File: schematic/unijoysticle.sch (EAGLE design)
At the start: 8 parts, among them IC1 4066N, IC2 4066N, IC3 4066N, J1 DB9, J2 DB9, J3 POWER_JACKSLT

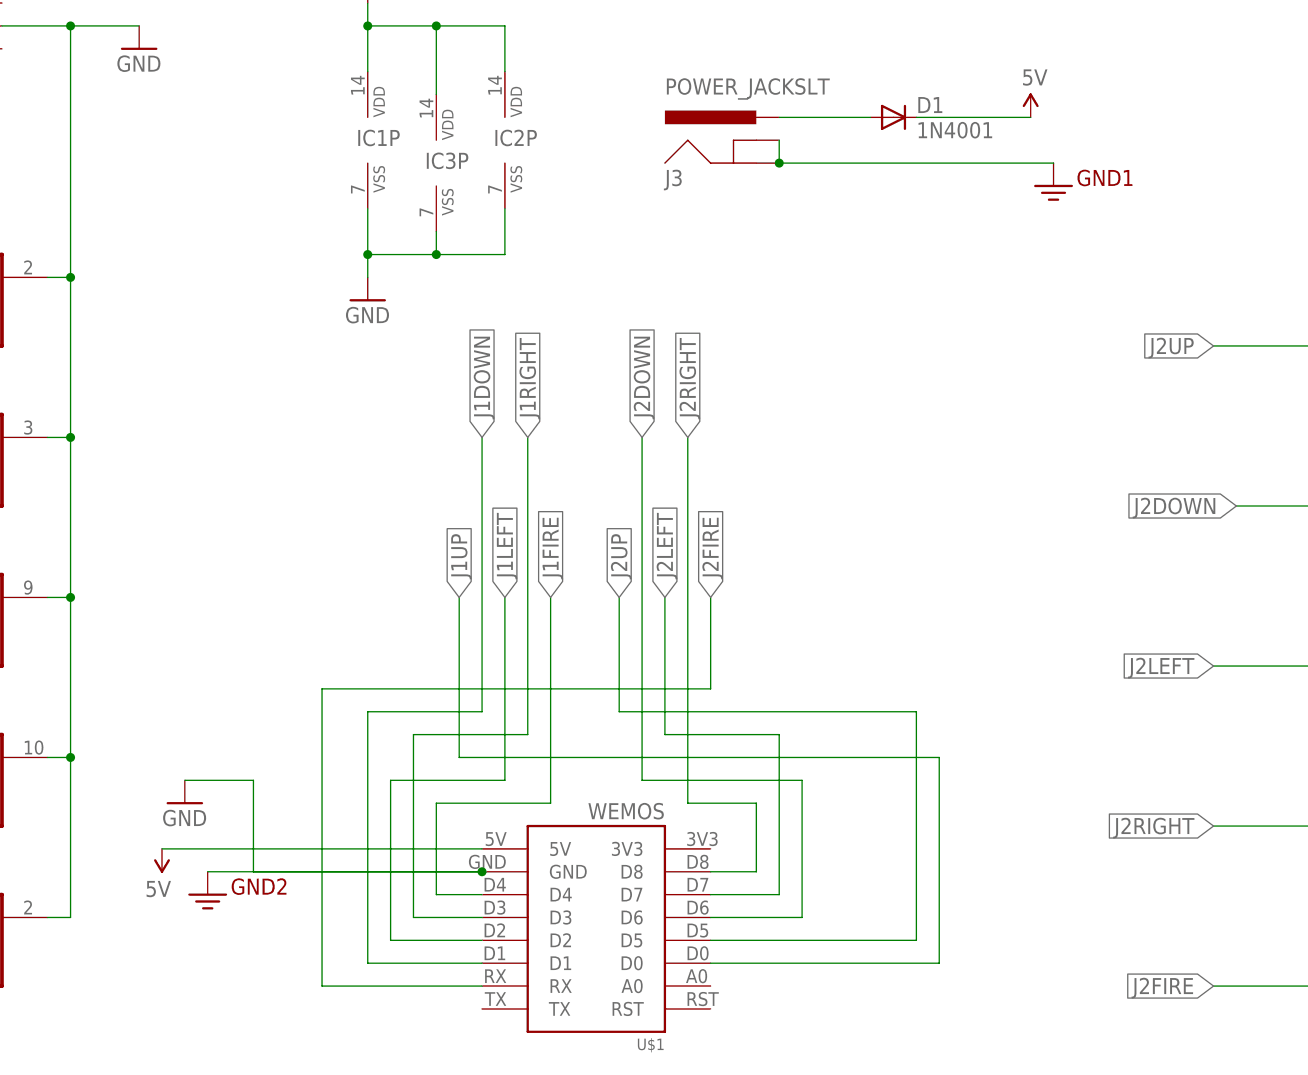
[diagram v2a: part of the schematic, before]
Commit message: sharing the same ground for all components
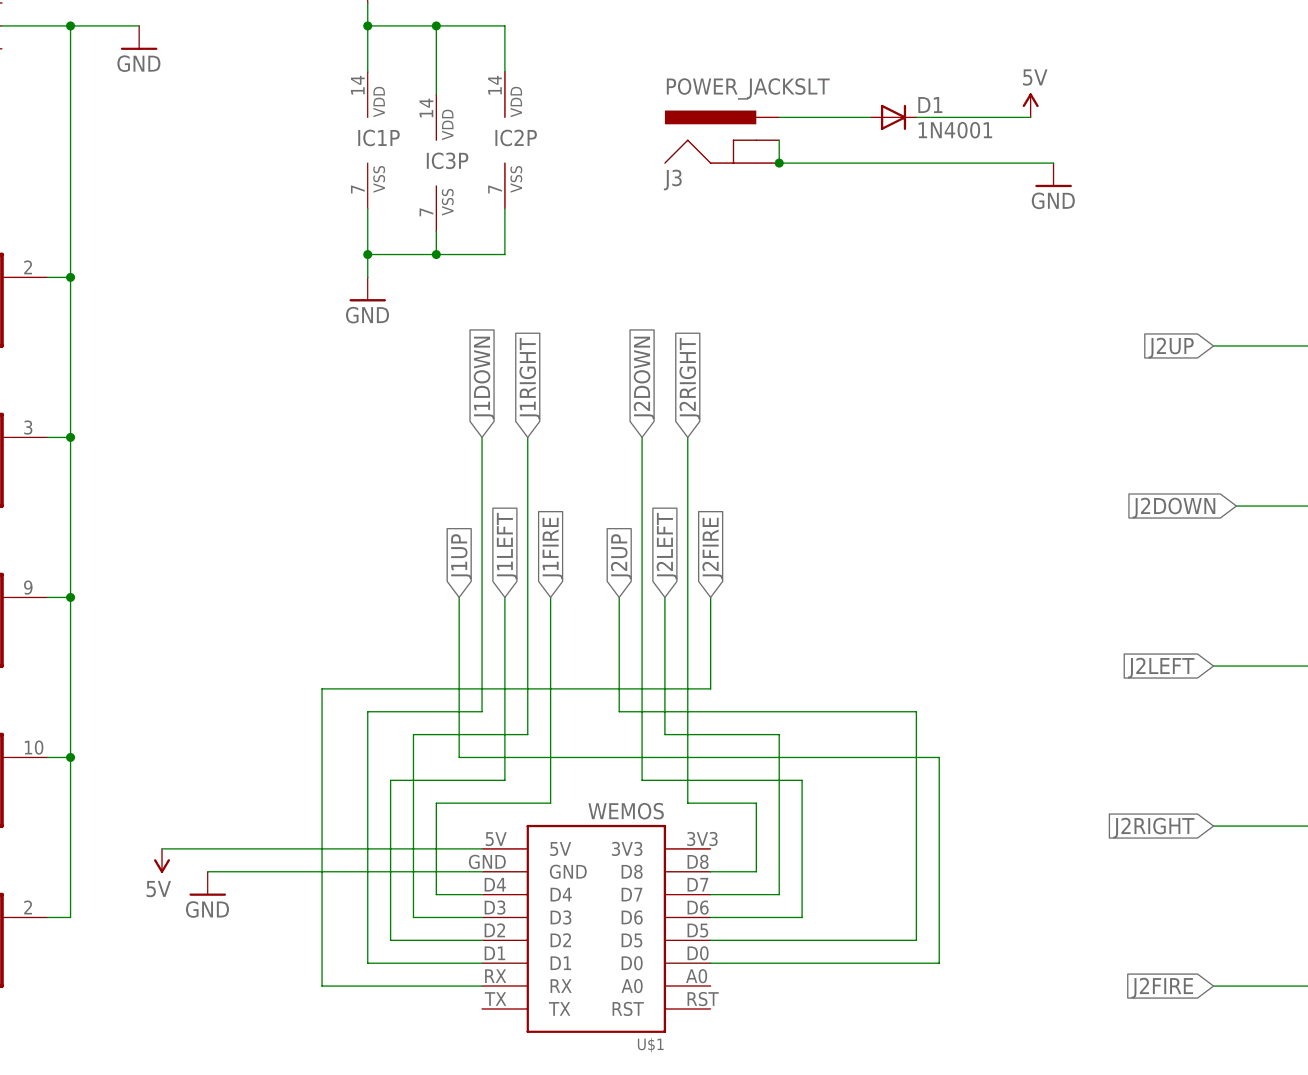
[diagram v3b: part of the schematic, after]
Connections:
- removed net 3.3V: J3.GND, J3.GNDBREAK
- net GND: now also J3.GND, J3.GNDBREAK
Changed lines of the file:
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@@
 <part name="SUPPLY1" library="SparkFun-Aesthetics" deviceset="5V" device=""/>
 <part name="SUPPLY2" library="SparkFun-Aesthetics" deviceset="5V" device=""/>
-<part name="GND1" library="SparkFun-Aesthetics" deviceset="GND2" device=""/>
-<part name="GND2" library="SparkFun-Aesthetics" deviceset="GND2" device=""/>
 <part name="J1" library="riq-connectors" deviceset="DB9" device="FEMALE" value="DB9">
 <attribute name="MF" value=""/>
@@
 <part name="GND6" library="SparkFun-Aesthetics" deviceset="GND" device=""/>
 <part name="U$1" library="1455413453956-wemos" deviceset="WEMOS" device=""/>
+<part name="GND1" library="supply1" deviceset="GND" device=""/>
 </parts>
 <sheets>
@@
 <instance part="IC1" gate="P" x="101.6" y="142.24"/>
 <instance part="IC3" gate="P" x="109.22" y="139.7"/>
-<instance part="GND3" gate="1" x="81.28" y="68.58"/>
+<instance part="GND3" gate="1" x="83.82" y="58.42"/>
 <instance part="GND4" gate="1" x="101.6" y="124.46"/>
 <instance part="IC2" gate="A" x="53.34" y="53.34">
@@
 <instance part="SUPPLY1" gate="G$1" x="175.26" y="144.78"/>
 <instance part="SUPPLY2" gate="G$1" x="78.74" y="63.5" rot="R180"/>
-<instance part="GND1" gate="G$1" x="177.8" y="137.16"/>
-<instance part="GND2" gate="G$1" x="83.82" y="58.42"/>
 <instance part="J1" gate="G$1" x="53.34" y="157.48">
 <attribute name="OC_NEWARK" x="53.34" y="157.48" size="1.778" layer="96" display="off"/>
@@
 <instance part="GND6" gate="1" x="76.2" y="152.4"/>
 <instance part="U$1" gate="G$1" x="134.62" y="66.04" rot="R180"/>
+<instance part="GND1" gate="1" x="177.8" y="137.16"/>
 </instances>
 <busses>
@@
 <segment>
 <pinref part="GND3" gate="1" pin="GND"/>
-<pinref part="GND2" gate="G$1" pin="3.3V"/>
+<pinref part="U$1" gate="G$1" pin="GND"/>
 <wire x1="83.82" y1="60.96" x2="114.3" y2="60.96" width="0.1524" layer="91"/>
-<pinref part="U$1" gate="G$1" pin="GND"/>
-<wire x1="81.28" y1="71.12" x2="88.9" y2="71.12" width="0.1524" layer="91"/>
-<wire x1="88.9" y1="71.12" x2="88.9" y2="60.96" width="0.1524" layer="91"/>
-<wire x1="88.9" y1="60.96" x2="114.3" y2="60.96" width="0.1524" layer="91"/>
-<junction x="114.3" y="60.96"/>
 </segment>
 <segment>
@@
 <pinref part="GND6" gate="1" pin="GND"/>
 </segment>
+<segment>
+<wire x1="147.32" y1="142.24" x2="147.32" y2="139.7" width="0.1524" layer="91"/>
+<wire x1="147.32" y1="139.7" x2="177.8" y2="139.7" width="0.1524" layer="91"/>
+<pinref part="J3" gate="G$1" pin="GNDBREAK"/>
+<pinref part="J3" gate="G$1" pin="GND"/>
+<junction x="147.32" y="139.7"/>
+<pinref part="GND1" gate="1" pin="GND"/>
+</segment>
 </net>
 <net name="VCC" class="0">
@@
 </segment>
 </net>
-<net name="3.3V" class="0">
-<segment>
-<wire x1="147.32" y1="142.24" x2="147.32" y2="139.7" width="0.1524" layer="91"/>
-<wire x1="147.32" y1="139.7" x2="177.8" y2="139.7" width="0.1524" layer="91"/>
-<pinref part="GND1" gate="G$1" pin="3.3V"/>
-<pinref part="J3" gate="G$1" pin="GNDBREAK"/>
-<pinref part="J3" gate="G$1" pin="GND"/>
-<junction x="147.32" y="139.7"/>
-</segment>
-</net>

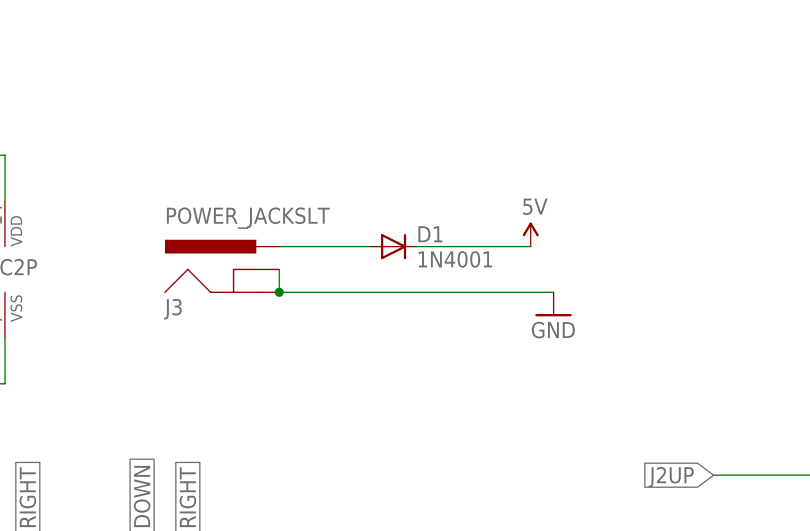
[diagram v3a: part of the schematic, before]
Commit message: removed diode
apparently not needed:
http://forum.wemos.cc/topic/343/power-the-board-with-both-usb-and-vin-pin-at-the-same-time
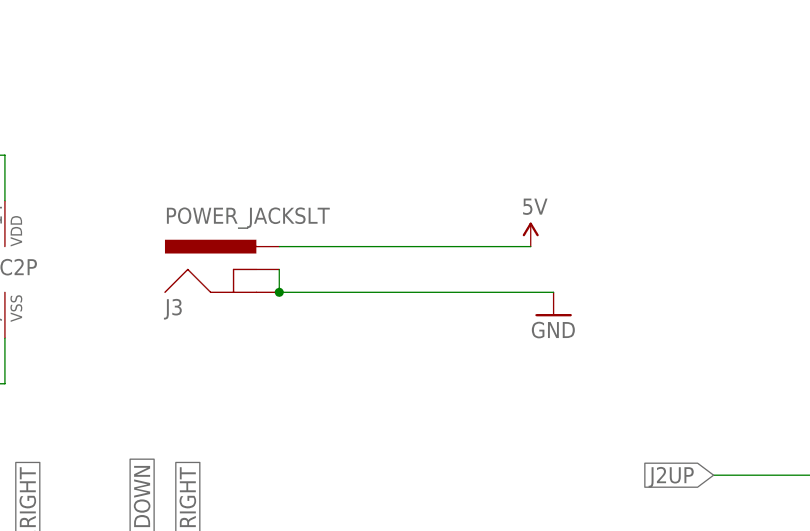
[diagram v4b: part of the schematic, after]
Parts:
- removed D1: 1N4001, diode:1N4004
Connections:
- removed net N$23: D1.A, J3.PWR
- net 5V: now also J3.PWR; no longer D1.C
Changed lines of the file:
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@@
 <attribute name="OC_NEWARK" value="76C3574"/>
-</part>
-<part name="D1" library="diode" deviceset="1N4004" device="" value="1N4001">
-<attribute name="MF" value="NTE ELECTRONICS"/>
-<attribute name="MPN" value="1N4001"/>
-<attribute name="OC_NEWARK" value="10M8464"/>
 </part>
 <part name="SUPPLY1" library="SparkFun-Aesthetics" deviceset="5V" device=""/>
@@
 <instance part="IC2" gate="B" x="233.68" y="50.8"/>
 <instance part="IC2" gate="P" x="116.84" y="142.24"/>
-<instance part="D1" gate="1" x="160.02" y="144.78">
-<attribute name="OC_NEWARK" x="160.02" y="144.78" size="1.778" layer="96" display="off"/>
-<attribute name="MF" x="160.02" y="144.78" size="1.778" layer="96" display="off"/>
-<attribute name="MPN" x="160.02" y="144.78" size="1.778" layer="96" display="off"/>
-</instance>
 <instance part="SUPPLY1" gate="G$1" x="175.26" y="144.78"/>
 <instance part="SUPPLY2" gate="G$1" x="78.74" y="63.5" rot="R180"/>
@@
 </segment>
 </net>
-<net name="N$23" class="1">
-<segment>
-<wire x1="147.32" y1="144.78" x2="157.48" y2="144.78" width="0.1524" layer="91"/>
-<pinref part="D1" gate="1" pin="A"/>
+<net name="5V" class="0">
+<segment>
+<pinref part="SUPPLY1" gate="G$1" pin="5V"/>
+<wire x1="147.32" y1="144.78" x2="175.26" y2="144.78" width="0.1524" layer="91"/>
 <pinref part="J3" gate="G$1" pin="PWR"/>
 </segment>
-</net>
-<net name="5V" class="0">
-<segment>
-<wire x1="162.56" y1="144.78" x2="175.26" y2="144.78" width="0.1524" layer="91"/>
-<pinref part="D1" gate="1" pin="C"/>
-<pinref part="SUPPLY1" gate="G$1" pin="5V"/>
-</segment>
-<segment>
+<segment>

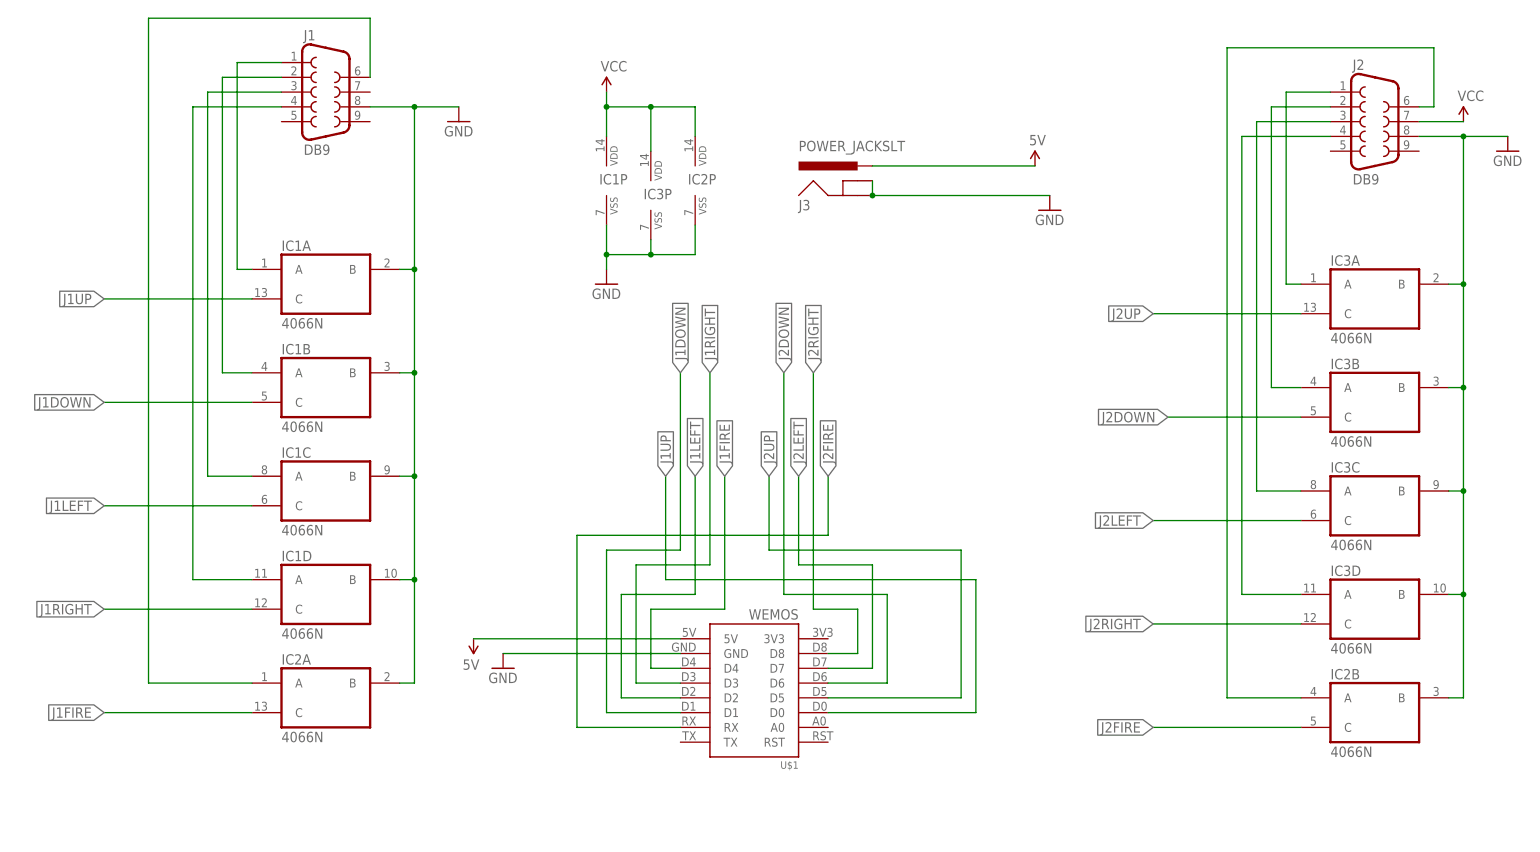
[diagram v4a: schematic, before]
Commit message: simplified board...
no more barrel jack for the D1 Mini version
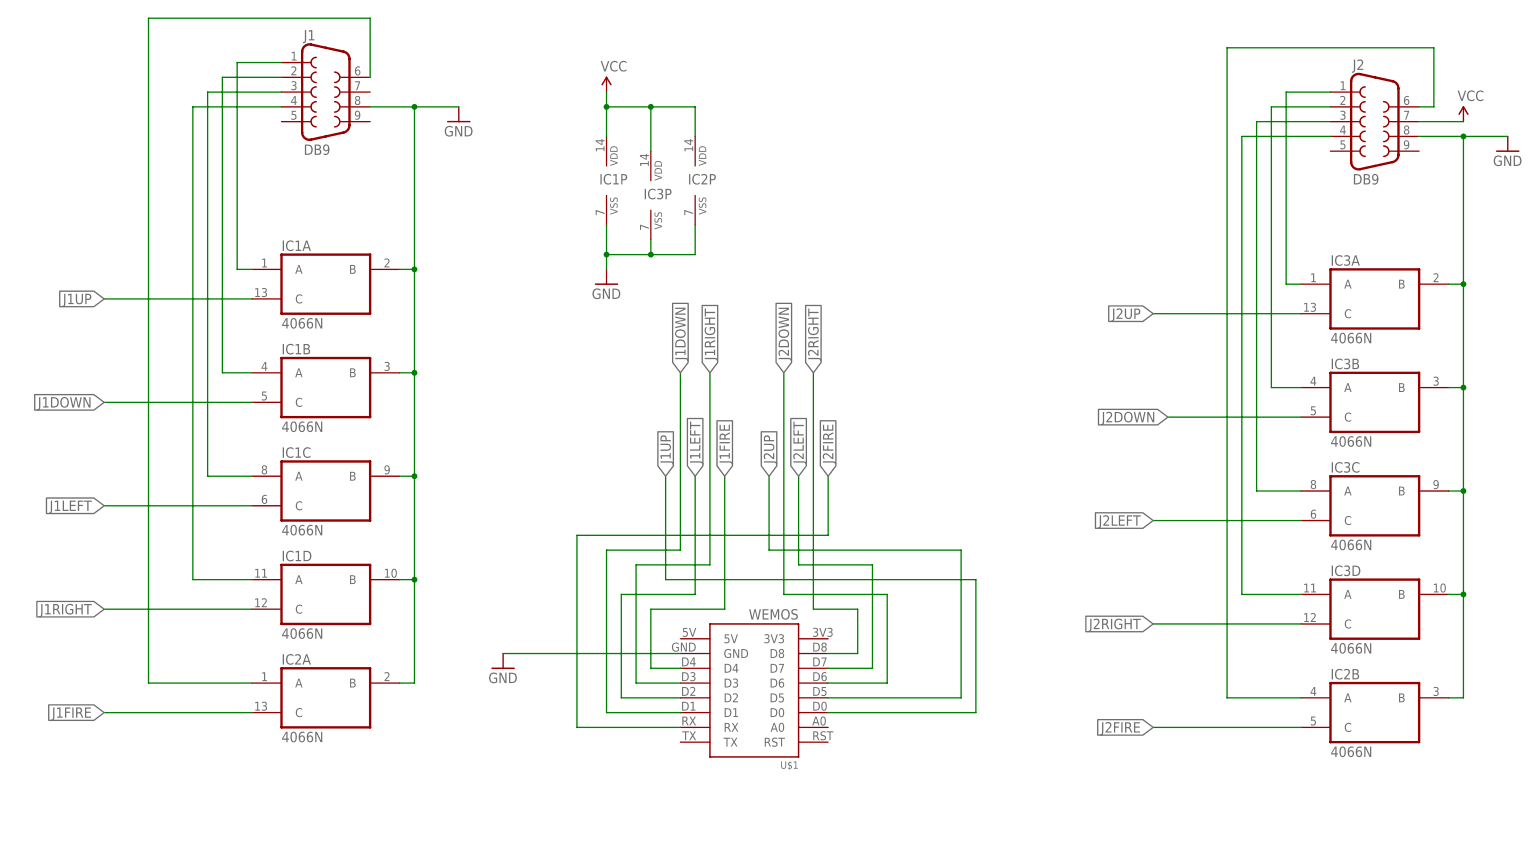
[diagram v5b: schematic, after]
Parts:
- removed J3: POWER_JACKSLT, SparkFun-Connectors:POWER_JACKSLT
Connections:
- removed net 5V: J3.PWR, U$1.5V
- net GND: no longer J3.GND, J3.GNDBREAK
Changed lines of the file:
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@@
 <attribute name="OC_NEWARK" value="76C3574"/>
 </part>
-<part name="SUPPLY1" library="SparkFun-Aesthetics" deviceset="5V" device=""/>
-<part name="SUPPLY2" library="SparkFun-Aesthetics" deviceset="5V" device=""/>
 <part name="J1" library="riq-connectors" deviceset="DB9" device="FEMALE" value="DB9">
 <attribute name="MF" value=""/>
@@
 </part>
 <part name="FRAME1" library="SparkFun-Aesthetics" deviceset="FRAME-A4L" device=""/>
-<part name="J3" library="SparkFun-Connectors" deviceset="POWER_JACK" device="SLT"/>
 <part name="SUPPLY3" library="SparkFun-Aesthetics" deviceset="VCC" device=""/>
 <part name="SUPPLY4" library="SparkFun-Aesthetics" deviceset="VCC" device=""/>
@@
 <part name="GND6" library="SparkFun-Aesthetics" deviceset="GND" device=""/>
 <part name="U$1" library="1455413453956-wemos" deviceset="WEMOS" device=""/>
-<part name="GND1" library="supply1" deviceset="GND" device=""/>
 </parts>
 <sheets>
@@
 <instance part="IC2" gate="B" x="233.68" y="50.8"/>
 <instance part="IC2" gate="P" x="116.84" y="142.24"/>
-<instance part="SUPPLY1" gate="G$1" x="175.26" y="144.78"/>
-<instance part="SUPPLY2" gate="G$1" x="78.74" y="63.5" rot="R180"/>
 <instance part="J1" gate="G$1" x="53.34" y="157.48">
 <attribute name="OC_NEWARK" x="53.34" y="157.48" size="1.778" layer="96" display="off"/>
@@
 </instance>
 <instance part="FRAME1" gate="G$1" x="0" y="0"/>
-<instance part="J3" gate="G$1" x="144.78" y="137.16"/>
 <instance part="SUPPLY3" gate="G$1" x="248.92" y="152.4"/>
 <instance part="SUPPLY4" gate="G$1" x="101.6" y="157.48"/>
@@
 <instance part="GND6" gate="1" x="76.2" y="152.4"/>
 <instance part="U$1" gate="G$1" x="134.62" y="66.04" rot="R180"/>
-<instance part="GND1" gate="1" x="177.8" y="137.16"/>
 </instances>
 <busses>
@@
 <pinref part="GND6" gate="1" pin="GND"/>
 </segment>
-<segment>
-<wire x1="147.32" y1="142.24" x2="147.32" y2="139.7" width="0.1524" layer="91"/>
-<wire x1="147.32" y1="139.7" x2="177.8" y2="139.7" width="0.1524" layer="91"/>
-<pinref part="J3" gate="G$1" pin="GNDBREAK"/>
-<pinref part="J3" gate="G$1" pin="GND"/>
-<junction x="147.32" y="139.7"/>
-<pinref part="GND1" gate="1" pin="GND"/>
-</segment>
 </net>
 <net name="VCC" class="0">
@@
 </segment>
 </net>
-<net name="5V" class="0">
-<segment>
-<pinref part="SUPPLY1" gate="G$1" pin="5V"/>
-<wire x1="147.32" y1="144.78" x2="175.26" y2="144.78" width="0.1524" layer="91"/>
-<pinref part="J3" gate="G$1" pin="PWR"/>
-</segment>
-<segment>
-<pinref part="SUPPLY2" gate="G$1" pin="5V"/>
-<wire x1="78.74" y1="63.5" x2="114.3" y2="63.5" width="0.1524" layer="91"/>
-<pinref part="U$1" gate="G$1" pin="5V"/>
-</segment>
-</net>
